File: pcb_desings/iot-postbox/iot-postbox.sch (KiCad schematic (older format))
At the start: 17 parts, among them J1 Switch_1, J2 Switch_2, J3 Battery, U1 ESP-12F, U2 TTL_to_USB

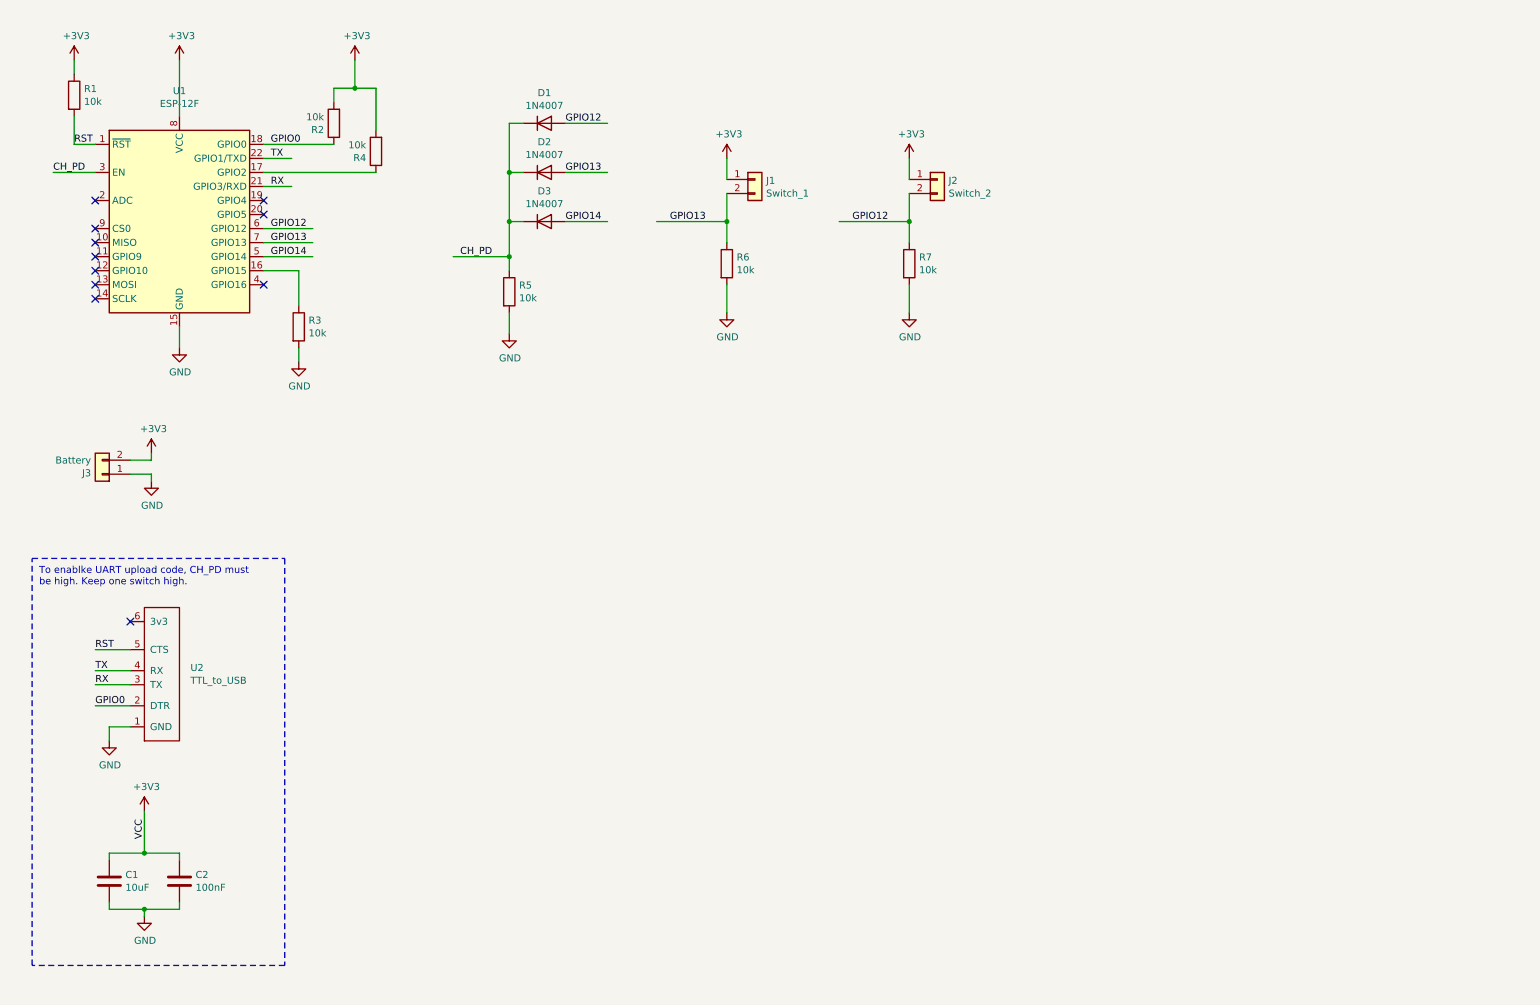
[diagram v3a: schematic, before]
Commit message: Add power and chargin management for iot-postbox pcb
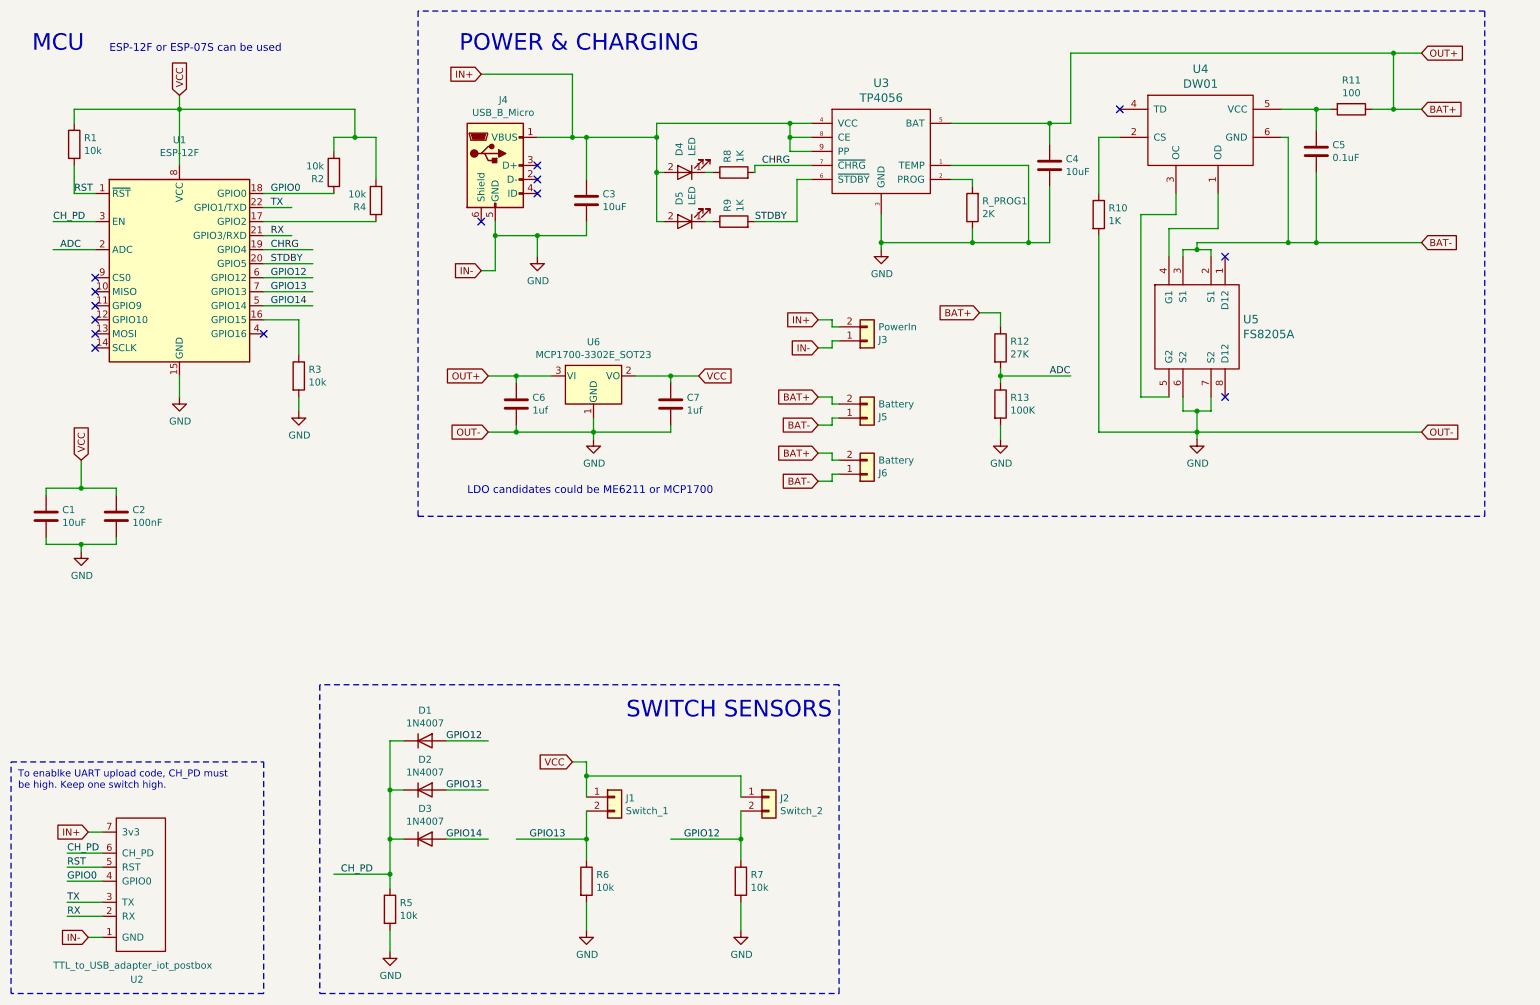
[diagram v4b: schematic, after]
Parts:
- removed U2: TTL_to_USB, Connector_PinHeader_2.54mm:PinHeader_1x06_P2.54mm_Vertical, symbol iot-postbox:TTL_to_USB
- added C3, C4: 10uF, Capacitor_SMD:C_0805_2012Metric, symbol charger_stepup-cache:C
- added C5: 0.1uF, Capacitor_SMD:C_0805_2012Metric, symbol charger_stepup-cache:C
- added C6, C7: 1uf, Capacitor_SMD:C_0805_2012Metric, symbol charger_stepup-cache:C
- added D4, D5: LED, LED_SMD:LED_0805_2012Metric, symbol charger_stepup-cache:LED
- added J4: USB_B_Micro, Connector_USB:USB_Micro-B_Amphenol_10118194_Horizontal, symbol Connector:USB_B_Micro
- added J5: Battery, Connector_JST:JST_PH_S2B-PH-SM4-TB_1x02-1MP_P2.00mm_Horizontal, symbol Connector_Generic:Conn_01x02
- added J6: Battery, Connector_PinHeader_2.54mm:PinHeader_1x02_P2.54mm_Horizontal, symbol Connector_Generic:Conn_01x02
- added R10, R8, R9: 1K, Resistor_SMD:R_0805_2012Metric, symbol charger_stepup-cache:R
- added R11: 100, Resistor_SMD:R_0805_2012Metric, symbol charger_stepup-cache:R
- added R12: 27K, Resistor_SMD:R_0805_2012Metric, symbol charger_stepup-cache:R
- added R13: 100K, Resistor_SMD:R_0805_2012Metric, symbol charger_stepup-cache:R
- added R_PROG1: 2K, Resistor_SMD:R_0805_2012Metric, symbol charger_stepup-cache:R
- added U2: TTL_to_USB_adapter_iot_postbox, ttl_to_usb_adapter:TTL_to_USB_PinHeader, symbol ttl_to_usb_adapter:TTL_to_USB_adapter_iot_postbox
- added U3: TP4056, lib:TP4056_SOP-8-PP, symbol charger_stepup-cache:TP4056
- added U4: DW01, Package_TO_SOT_SMD:SOT-23-6_Handsoldering, symbol charger_stepup-cache:DW01
- added U5: FS8205A, Package_SO:TSSOP-8_4.4x3mm_P0.65mm, symbol charger_stepup-cache:FS8205A
- added U6: MCP1700-3302E_SOT23, Package_TO_SOT_SMD:SOT-23, symbol Regulator_Linear:MCP1700-3302E_SOT23
- J3: value Battery -> PowerIn; footprint Connector_PinHeader_2.54mm:PinHeader_1x02_P2.54mm_Vertical -> Connector_PinHeader_2.54mm:PinHeader_1x02_P2.54mm_Horizontal
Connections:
- net labels added: ADC, BAT+, BAT-, CHRG, IN+, IN-, OUT+, OUT-, STDBY
- net labels removed: +3V3
- wire segments 63 -> 189
- no-connect marks 11 -> 14
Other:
- note added: "ESP-12F or ESP-07S can be used"
- note added: "LDO candidates could be ME6211 or MCP1700"
- note added: "MCU"
- note added: "POWER & CHARGING"
- note added: "SWITCH SENSORS"
- moved on the sheet: C1, C2, D1, D2, D3, J1, J2, J3, R1, R2, R3, R4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

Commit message: Updated iot-postbox pcb to v0.0
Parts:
- removed U2: TTL_to_USB_adapter_iot_postbox, ttl_to_usb_adapter:TTL_to_USB_PinHeader, symbol ttl_to_usb_adapter:TTL_to_USB_adapter_iot_postbox
- added SW1: POWER, MSK12C02:1P2T_SPDT_MSK-C02_7pin, symbol Switch:SW_SPDT
- added U2: TTL_UART_adapter_iot_postbox, Connector_PinHeader_2.54mm:PinHeader_1x07_P2.54mm_Vertical, symbol ttl_to_usb_adapter:TTL_UART_adapter_iot_postbox
- J3, J6: footprint Connector_PinHeader_2.54mm:PinHeader_1x02_P2.54mm_Horizontal -> Connector_PinHeader_2.54mm:PinHeader_1x02_P2.54mm_Vertical
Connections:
- net labels added: OUT
- wire segments 189 -> 190
- no-connect marks 14 -> 15
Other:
- moved on the sheet: C6, C7, J3, J5, J6, R12, R13, U6

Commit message: Updated iotpostbox sch to v0.1 and pcb to v0.2. Fixed tp4056 radiator and updated battery adc resistances
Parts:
- D4: value LED -> CHRG
- D5: value LED -> STDBY
- R1, R2, R3, R4, R5, R6, R7: value 10k -> 10K
- R11: value 100 -> 100R
- R12: value 27K -> 1M
- R13: value 100K -> 300K
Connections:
- wire segments 190 -> 188
- no-connect marks 15 -> 16
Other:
- note added: "ADC esp8266 max. 1v\nVoltage divider with max. 4.333v BAT+"
- note added: "BATTERY SENSOR"
- moved on the sheet: D5, R12, R13, R9
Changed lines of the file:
@@
 Title "IoT-PostBox"
 Date "2021-07-08"
-Rev "v0.0"
+Rev "v0.1"
 Comp ""
 Comment1 "https://github.com/paclema/iot-postbox"
@@
 P 1050 1600
 F 0 "R1" H 1120 1646 50  0000 L CNN
-F 1 "10k" H 1120 1555 50  0000 L CNN
+F 1 "10K" H 1120 1555 50  0000 L CNN
 F 2 "Resistor_SMD:R_0805_2012Metric" V 980 1600 50  0001 C CNN
 F 3 "~" H 1050 1600 50  0001 C CNN
@@
 P 3300 7050
 F 0 "R5" H 3370 7096 50  0000 L CNN
-F 1 "10k" H 3370 7005 50  0000 L CNN
+F 1 "10K" H 3370 7005 50  0000 L CNN
 F 2 "Resistor_SMD:R_0805_2012Metric" V 3230 7050 50  0001 C CNN
 F 3 "~" H 3300 7050 50  0001 C CNN
@@
 P 2650 3250
 F 0 "R3" H 2720 3296 50  0000 L CNN
-F 1 "10k" H 2720 3205 50  0000 L CNN
+F 1 "10K" H 2720 3205 50  0000 L CNN
 F 2 "Resistor_SMD:R_0805_2012Metric" V 2580 3250 50  0001 C CNN
 F 3 "~" H 2650 3250 50  0001 C CNN
@@
 P 4700 6850
 F 0 "R6" H 4770 6896 50  0000 L CNN
-F 1 "10k" H 4770 6805 50  0000 L CNN
+F 1 "10K" H 4770 6805 50  0000 L CNN
 F 2 "Resistor_SMD:R_0805_2012Metric" V 4630 6850 50  0001 C CNN
 F 3 "~" H 4700 6850 50  0001 C CNN
@@
 P 5800 6850
 F 0 "R7" H 5870 6896 50  0000 L CNN
-F 1 "10k" H 5870 6805 50  0000 L CNN
+F 1 "10K" H 5870 6805 50  0000 L CNN
 F 2 "Resistor_SMD:R_0805_2012Metric" V 5730 6850 50  0001 C CNN
 F 3 "~" H 5800 6850 50  0001 C CNN
@@
 P 2900 1800
 F 0 "R2" H 2970 1846 50  0000 L CNN
-F 1 "10k" H 2970 1755 50  0000 L CNN
+F 1 "10K" H 2970 1755 50  0000 L CNN
 F 2 "Resistor_SMD:R_0805_2012Metric" V 2830 1800 50  0001 C CNN
 F 3 "~" H 2900 1800 50  0001 C CNN
@@
 P 3200 2000
 F 0 "R4" H 3270 2046 50  0000 L CNN
-F 1 "10k" H 3270 1955 50  0000 L CNN
+F 1 "10K" H 3270 1955 50  0000 L CNN
 F 2 "Resistor_SMD:R_0805_2012Metric" V 3130 2000 50  0001 C CNN
 F 3 "~" H 3200 2000 50  0001 C CNN
@@
 L charger_stepup-cache:R R9
 U 1 1 60E36525
-P 5750 2150
-F 0 "R9" H 5820 2196 50  0000 L CNN
-F 1 "1K" H 5820 2105 50  0000 L CNN
-F 2 "Resistor_SMD:R_0805_2012Metric" V 5680 2150 50  0001 C CNN
-F 3 "" H 5750 2150 50  0001 C CNN
-	1    5750 2150
+P 5750 2300
+F 0 "R9" H 5820 2346 50  0000 L CNN
+F 1 "1K" H 5820 2255 50  0000 L CNN
+F 2 "Resistor_SMD:R_0805_2012Metric" V 5680 2300 50  0001 C CNN
+F 3 "" H 5750 2300 50  0001 C CNN
+	1    5750 2300
 	0    -1   -1   0
 $EndComp
@@
 L charger_stepup-cache:LED D5
 U 1 1 60E4D83A
-P 5400 2150
-F 0 "D5" V 5439 2033 50  0000 R CNN
-F 1 "LED" V 5348 2033 50  0000 R CNN
-F 2 "LED_SMD:LED_0805_2012Metric" H 5400 2150 50  0001 C CNN
-F 3 "" H 5400 2150 50  0001 C CNN
-	1    5400 2150
+P 5400 2300
+F 0 "D5" H 5500 2450 50  0000 R CNN
+F 1 "STDBY" H 5500 2550 50  0000 R CNN
+F 2 "LED_SMD:LED_0805_2012Metric" H 5400 2300 50  0001 C CNN
+F 3 "" H 5400 2300 50  0001 C CNN
+	1    5400 2300
 	-1   0    0    1
 $EndComp
 Wire Wire Line
-	5550 2150 5600 2150
+	5550 2300 5600 2300
 $Comp
 L charger_stepup-cache:R R8
@@
 U 1 1 60E53CB0
 P 5400 1800
-F 0 "D4" V 5439 1683 50  0000 R CNN
-F 1 "LED" V 5348 1683 50  0000 R CNN
+F 0 "D4" H 5500 1950 50  0000 R CNN
+F 1 "CHRG" H 5500 2050 50  0000 R CNN
 F 2 "LED_SMD:LED_0805_2012Metric" H 5400 1800 50  0001 C CNN
 F 3 "" H 5400 1800 50  0001 C CNN
@@
 	5200 1800 5250 1800
 Wire Wire Line
-	5200 1800 5200 2150
-Wire Wire Line
-	5200 2150 5250 2150
-Connection ~ 5200 1800
+	5200 2300 5250 2300
 Wire Wire Line
 	5200 1550 5200 1450
@@
 Wire Wire Line
 	5900 1800 5900 1750
-Wire Wire Line
-	6200 2150 6200 1850
 Wire Wire Line
 	6200 1850 6300 1850
@@
 P 10150 1350
 F 0 "R11" V 9943 1350 50  0000 C CNN
-F 1 "100" V 10034 1350 50  0000 C CNN
+F 1 "100R" V 10034 1350 50  0000 C CNN
 F 2 "Resistor_SMD:R_0805_2012Metric" V 10080 1350 50  0001 C CNN
 F 3 "" H 10150 1350 50  0001 C CNN
@@
 Wire Notes Line
 	2800 7650 6500 7650
-Wire Notes Line
-	6500 7650 6500 5450
-Wire Notes Line
-	6500 5450 2800 5450
-Wire Notes Line
-	2800 5450 2800 7650
-Text Notes 6450 5700 2    118  ~ 0
+Text Notes 6350 5600 2    118  ~ 0
 SWITCH SENSORS
-Wire Wire Line
-	6300 1650 6150 1650
-Wire Wire Line
-	6150 1650 6150 1550
-Connection ~ 6150 1550
 Wire Wire Line
 	1200 2350 900  2350
 Text Label 950  2350 0    50   ~ 0
 ADC
-Text GLabel 7600 2850 0    50   Input ~ 0
+Text GLabel 10050 5050 0    50   Input ~ 0
 BAT+
 $Comp
 L charger_stepup-cache:R R12
 U 1 1 61025CCF
-P 7750 3100
-F 0 "R12" H 7820 3146 50  0000 L CNN
-F 1 "27K" H 7820 3055 50  0000 L CNN
-F 2 "Resistor_SMD:R_0805_2012Metric" V 7680 3100 50  0001 C CNN
-F 3 "" H 7750 3100 50  0001 C CNN
-	1    7750 3100
+P 10200 5300
+F 0 "R12" H 10270 5346 50  0000 L CNN
+F 1 "1M" H 10270 5255 50  0000 L CNN
+F 2 "Resistor_SMD:R_0805_2012Metric" V 10130 5300 50  0001 C CNN
+F 3 "" H 10200 5300 50  0001 C CNN
+	1    10200 5300
 	1    0    0    -1
 $EndComp
@@
 L charger_stepup-cache:R R13
 U 1 1 61026824
-P 7750 3500
-F 0 "R13" H 7820 3546 50  0000 L CNN
-F 1 "100K" H 7820 3455 50  0000 L CNN
-F 2 "Resistor_SMD:R_0805_2012Metric" V 7680 3500 50  0001 C CNN
-F 3 "" H 7750 3500 50  0001 C CNN
-	1    7750 3500
-	1    0    0    -1
-$EndComp
-Wire Wire Line
-	7600 2850 7750 2850
-Wire Wire Line
-	7750 2850 7750 2950
-Wire Wire Line
-	7750 3250 7750 3300
-Wire Wire Line
-	7750 3650 7750 3750
+P 10200 5700
+F 0 "R13" H 10270 5746 50  0000 L CNN
+F 1 "300K" H 10270 5655 50  0000 L CNN
+F 2 "Resistor_SMD:R_0805_2012Metric" V 10130 5700 50  0001 C CNN
+F 3 "" H 10200 5700 50  0001 C CNN
+	1    10200 5700
+	1    0    0    -1
+$EndComp
+Wire Wire Line
+	10050 5050 10200 5050
+Wire Wire Line
+	10200 5050 10200 5150
+Wire Wire Line
+	10200 5450 10200 5500
+Wire Wire Line
+	10200 5850 10200 5950
 $Comp
 L power:GND #PWR015
 U 1 1 61042377
-P 7750 3750
-F 0 "#PWR015" H 7750 3500 50  0001 C CNN
-F 1 "GND" H 7755 3577 50  0000 C CNN
-F 2 "" H 7750 3750 50  0001 C CNN
-F 3 "" H 7750 3750 50  0001 C CNN
-	1    7750 3750
-	1    0    0    -1
-$EndComp
-Text Label 8100 3300 0    50   ~ 0
+P 10200 5950
+F 0 "#PWR015" H 10200 5700 50  0001 C CNN
+F 1 "GND" H 10205 5777 50  0000 C CNN
+F 2 "" H 10200 5950 50  0001 C CNN
+F 3 "" H 10200 5950 50  0001 C CNN
+	1    10200 5950
+	1    0    0    -1
+$EndComp
+Text Label 10550 5500 0    50   ~ 0
 ADC
 Wire Wire Line
-	7750 3300 8250 3300
-Connection ~ 7750 3300
-Wire Wire Line
-	7750 3300 7750 3350
+	10200 5500 10700 5500
+Connection ~ 10200 5500
+Wire Wire Line
+	10200 5500 10200 5550
 Wire Wire Line
 	2400 2350 2750 2350
@@
 Wire Wire Line
 	5900 1750 6300 1750
-Text Label 5900 2150 0    50   ~ 0
+Text Label 5900 2300 0    50   ~ 0
 STDBY
 Wire Wire Line
-	5900 2150 6200 2150
+	5900 2300 6200 2300
 $Comp
 L Regulator_Linear:MCP1700-3302E_SOT23 U6
@@
 	1    0    0    -1
 $EndComp
+NoConn ~ 6300 1650
+Text Notes 9600 6400 0    50   ~ 0
+ADC esp8266 max. 1v\nVoltage divider with max. 4.333v BAT+
+Wire Notes Line
+	9550 6450 9550 4700
+Wire Notes Line
+	9550 4700 11150 4700
+Wire Notes Line
+	11150 4700 11150 6450
+Wire Notes Line
+	9550 6450 11150 6450
+Wire Wire Line
+	6200 1850 6200 2300
+Wire Wire Line
+	5200 1800 5200 2300
+Connection ~ 5200 1800
+Text Notes 11100 4900 2    118  ~ 0
+BATTERY SENSOR
+Wire Notes Line
+	6500 5300 2800 5300
+Wire Notes Line
+	2800 5300 2800 7650
+Wire Notes Line
+	6500 5300 6500 7650
 $EndSCHEMATC

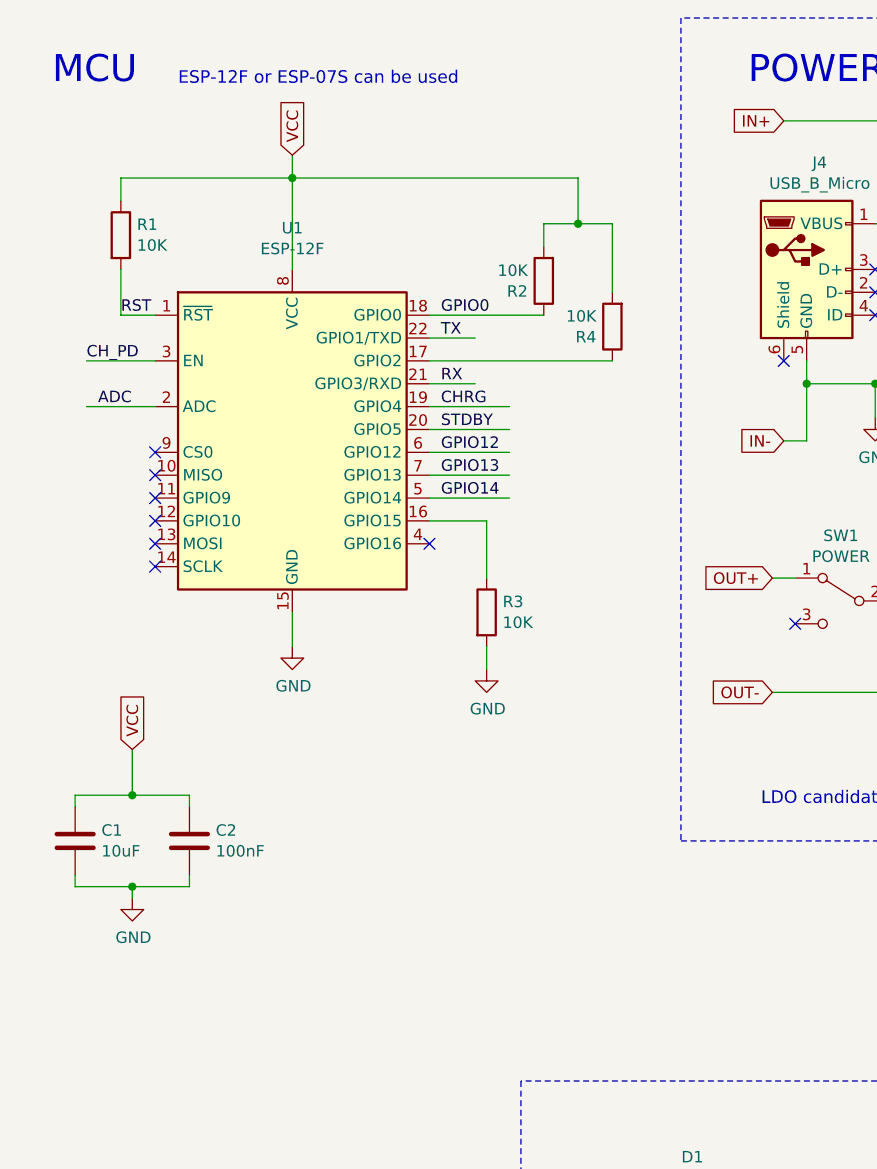
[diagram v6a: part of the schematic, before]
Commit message: For ESP-07s pull-ups/down resistors are not required
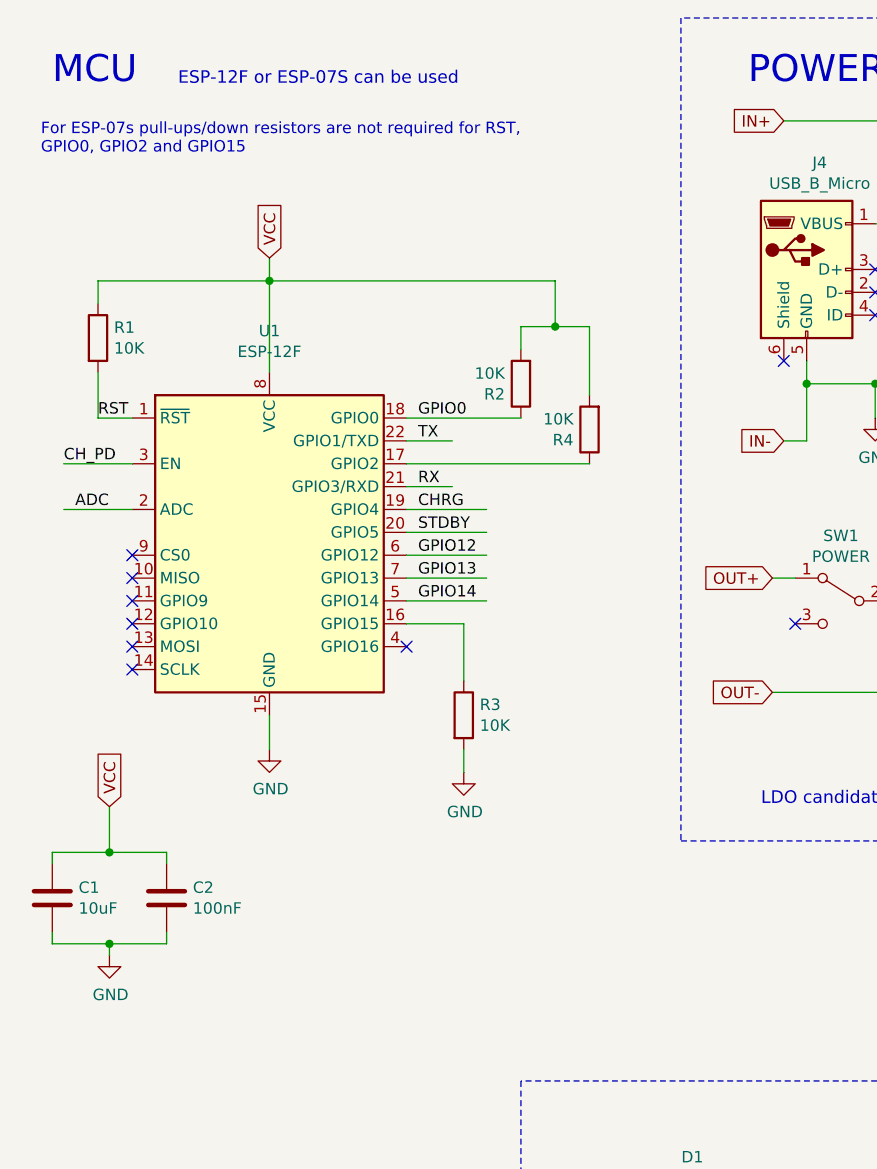
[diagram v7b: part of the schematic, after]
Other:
- note added: "For ESP-07s pull-ups/down resistors are not required for RST,\nGPIO0, GPIO2 and GPIO15"
- moved on the sheet: C1, C2, R1, R2, R3, R4, U1
